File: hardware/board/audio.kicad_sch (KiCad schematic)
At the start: 68 parts, among them J5 LineIn, J6 LineOut, J7 Headphone, U5 TPS7A20xxxDBV, U6 MAX98089ETN_T, Y2 12.288MHz

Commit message: hella footprints and trying out layouts
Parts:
- J5, J6: footprint Connector_Audio:Jack_3.5mm_CUI_SJ-3523-SMT_Horizontal -> Connector_Audio:Jack_3.5mm_CUI_SJ1-3525N_Horizontal
- J7: footprint ledaw:CUI_SJ-43514-SMT-TR -> ledaw:CUI_SJ-43514
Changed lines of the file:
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@@
 			)
 		)
-		(property "Footprint" "Connector_Audio:Jack_3.5mm_CUI_SJ-3523-SMT_Horizontal"
+		(property "Footprint" "Connector_Audio:Jack_3.5mm_CUI_SJ1-3525N_Horizontal"
 			(at 207.01 86.36 0)
 			(hide yes)
@@
 			)
 		)
-		(property "Footprint" "ledaw:CUI_SJ-43514-SMT-TR"
+		(property "Footprint" "ledaw:CUI_SJ-43514"
 			(at 207.01 107.95 0)
 			(hide yes)
@@
 			)
 		)
-		(property "Footprint" "Connector_Audio:Jack_3.5mm_CUI_SJ-3523-SMT_Horizontal"
+		(property "Footprint" "Connector_Audio:Jack_3.5mm_CUI_SJ1-3525N_Horizontal"
 			(at 71.12 107.95 0)
 			(hide yes)

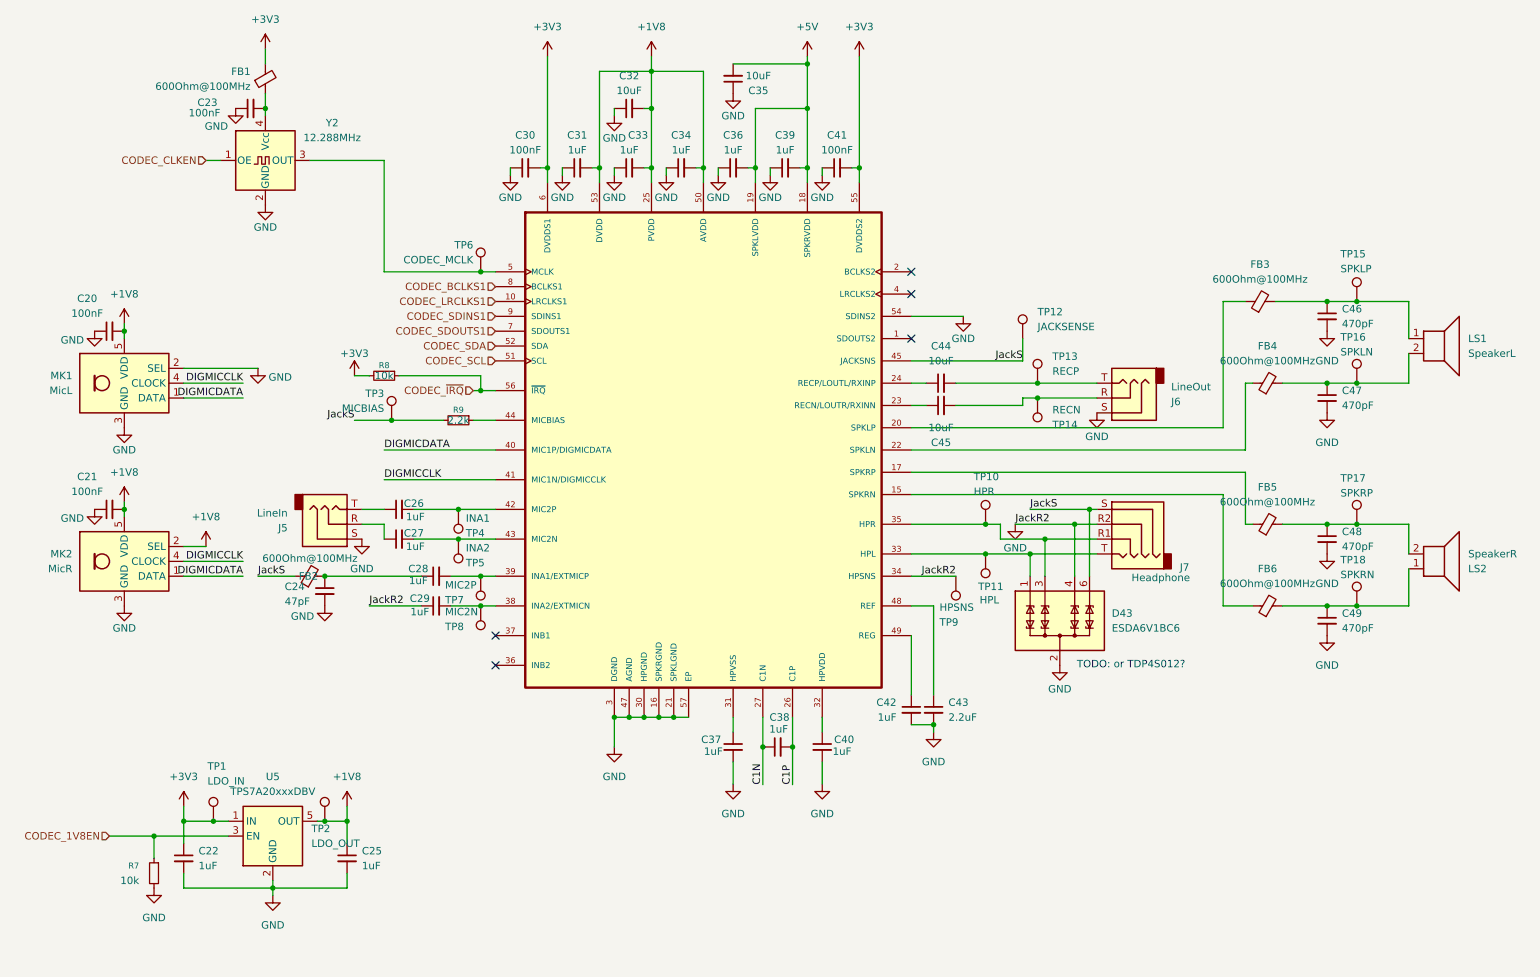
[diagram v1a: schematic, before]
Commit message: fix hpmic / linein mixup
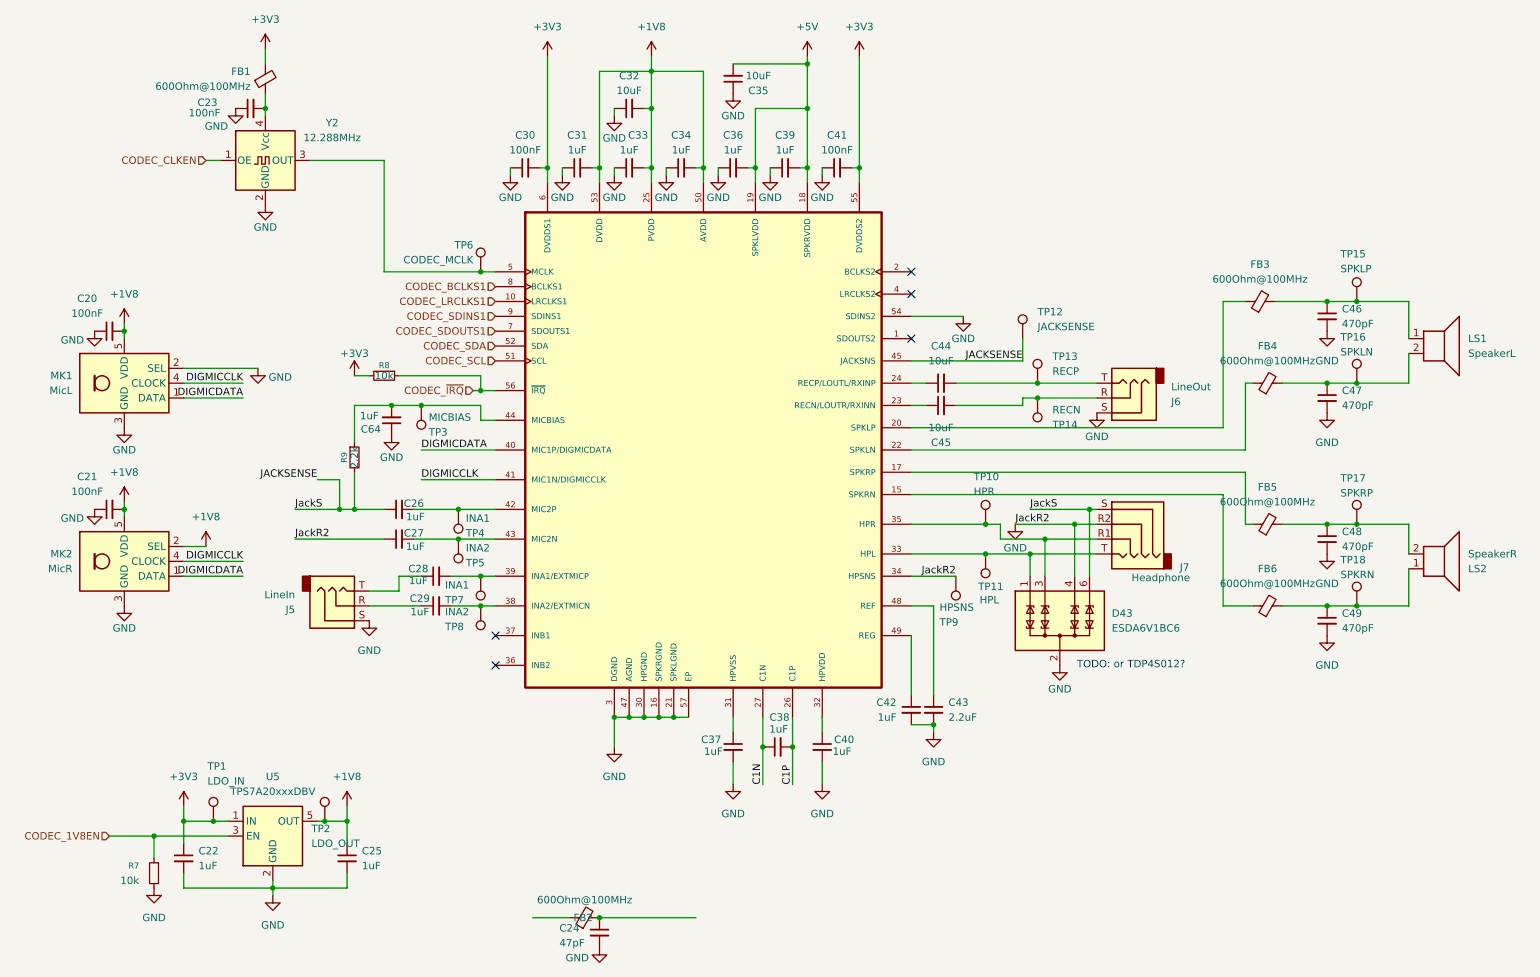
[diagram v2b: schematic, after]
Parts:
- added C64: 1uF, Capacitor_SMD:C_0805_2012Metric, symbol Device:C_Small
- TP7: value MIC2P -> INA1
- TP8: value MIC2N -> INA2
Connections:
- net GND: now also C27.1, C64.1; no longer C29.1
- net at C24.1, FB2.2: no longer C28.1
- net at J5.T: now also C28.1; no longer C26.1
- net at J5.R: now also C29.1; no longer C27.1
- net at R9.1, U6.44 (MICBIAS): now also TP3.1, C64.2
- net JackS renamed JACKSENSE
- net JACKSENSE: now also C26.1; no longer FB2.1, TP3.1

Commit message: reannoation with good linkage?
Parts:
- renumbered C35 to C201, C23 to C202, C32 to C203, C30 to C204, C31 to C205, C33 to C206, C34 to C207, C36 to C208, C39 to C209, C41 to C210, C46 to C211, C20 to C212, C44 to C213, C47 to C214, C45 to C215, C64 to C216, C21 to C217, C26 to C218, C27 to C219, C48 to C220, C28 to C221, C29 to C222, C49 to C223, C42 to C224, C43 to C225, C37 to C226, C38 to C227, C40 to C228, C22 to C229, C25 to C230, C24 to C231, D43 to D201, FB1 to FB201, FB3 to FB202, FB4 to FB203, FB5 to FB204, FB6 to FB205, FB2 to FB206, J6 to J201, J7 to J202, J5 to J203, LS1 to LS201, LS2 to LS202, MK1 to MK201, MK2 to MK202, R8 to R201, R9 to R202, R7 to R203, TP6 to TP201, TP15 to TP202, TP12 to TP203, TP13 to TP204, TP16 to TP205, TP14 to TP206, TP3 to TP207, TP4 to TP208, TP10 to TP209, TP17 to TP210, TP5 to TP211, TP11 to TP212, TP7 to TP213, TP9 to TP214, TP8 to TP215, TP18 to TP216, TP1 to TP217, TP2 to TP218, U6 to U201, U5 to U202, Y2 to Y201

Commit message: wip made a mistake adding micbias cap from hat
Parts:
- renumbered C216 to CX201
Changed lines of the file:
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@@
 		(in_pos_files yes)
 		(dnp no)
-		(property "Reference" "C216"
+		(property "Reference" "CX201"
 			(at 77.724 91.694 0)
 			(show_name no)
@@
 			(project "board"
 				(path "/dd13fd41-39ab-4435-9074-5024f1786746/bead49b4-6be4-481c-a37b-4cba7f02eadb"
-					(reference "C216")
+					(reference "CX201")
 					(unit 1)
 				)

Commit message: i think this is finally right
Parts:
- removed C231: 47pF, Capacitor_SMD:C_0805_2012Metric, symbol Device:C_Small
- removed FB206: 600Ohm@100MHz, Inductor_SMD:L_0805_2012Metric, symbol Device:FerriteBead_Small
- added C230: 47pF, Capacitor_SMD:C_0805_2012Metric, symbol Device:C_Small
- renumbered C217 to C216, C218 to C217, C219 to C218, C220 to C219, C221 to C220, C222 to C221, C223 to C222, C224 to C223, C225 to C224, C226 to C225, C227 to C226, C228 to C227, C229 to C228, C230 to C229

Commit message: speakers?
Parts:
- LS201, LS202: now not fitted
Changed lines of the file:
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@@
 		(on_board yes)
 		(in_pos_files yes)
-		(dnp no)
+		(dnp yes)
 		(property "Reference" "LS202"
 			(at 265.43 115.5701 0)
@@
 		(on_board yes)
 		(in_pos_files yes)
-		(dnp no)
+		(dnp yes)
 		(property "Reference" "LS201"
 			(at 265.43 76.1999 0)

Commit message: some big tim routing
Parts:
- renumbered C230 to C221, C221 to C222, C222 to C223, C223 to C224, C224 to C225, C225 to C226, C226 to C227, C227 to C228, C228 to C229, C229 to C230
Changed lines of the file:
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@@
 		(in_pos_files yes)
 		(dnp no)
-		(property "Reference" "C223"
+		(property "Reference" "C224"
 			(at 167.64 138.4362 0)
 			(show_name no)
@@
 			(project "board"
 				(path "/dd13fd41-39ab-4435-9074-5024f1786746/bead49b4-6be4-481c-a37b-4cba7f02eadb"
-					(reference "C223")
+					(reference "C224")
 					(unit 1)
 				)
@@
 		(in_pos_files yes)
 		(dnp no)
-		(property "Reference" "C225"
+		(property "Reference" "C226"
 			(at 137.668 144.78 0)
 			(show_name no)
@@
 			(project "board"
 				(path "/dd13fd41-39ab-4435-9074-5024f1786746/bead49b4-6be4-481c-a37b-4cba7f02eadb"
-					(reference "C225")
+					(reference "C226")
 					(unit 1)
 				)
@@
 		(in_pos_files yes)
 		(dnp no)
-		(property "Reference" "C227"
+		(property "Reference" "C228"
 			(at 156.972 144.78 0)
 			(show_name no)
@@
 			(project "board"
 				(path "/dd13fd41-39ab-4435-9074-5024f1786746/bead49b4-6be4-481c-a37b-4cba7f02eadb"
-					(reference "C227")
+					(reference "C228")
 					(unit 1)
 				)
@@
 		(dnp no)
 		(fields_autoplaced yes)
-		(property "Reference" "C222"
+		(property "Reference" "C223"
 			(at 243.84 123.1962 0)
 			(show_name no)
@@
 			(project "board"
 				(path "/dd13fd41-39ab-4435-9074-5024f1786746/bead49b4-6be4-481c-a37b-4cba7f02eadb"
-					(reference "C222")
+					(reference "C223")
 					(unit 1)
 				)
@@
 		(in_pos_files yes)
 		(dnp no)
-		(property "Reference" "C230"
+		(property "Reference" "C221"
 			(at 49.022 119.888 0)
 			(show_name no)
@@
 			(project "board"
 				(path "/dd13fd41-39ab-4435-9074-5024f1786746/bead49b4-6be4-481c-a37b-4cba7f02eadb"
-					(reference "C230")
+					(reference "C221")
 					(unit 1)
 				)
@@
 		(dnp no)
 		(fields_autoplaced yes)
-		(property "Reference" "C229"
+		(property "Reference" "C230"
 			(at 76.2 163.8362 0)
 			(show_name no)
@@
 			(project "board"
 				(path "/dd13fd41-39ab-4435-9074-5024f1786746/bead49b4-6be4-481c-a37b-4cba7f02eadb"
-					(reference "C229")
+					(reference "C230")
 					(unit 1)
 				)
@@
 		(dnp no)
 		(fields_autoplaced yes)
-		(property "Reference" "C224"
+		(property "Reference" "C225"
 			(at 176.53 138.4362 0)
 			(show_name no)
@@
 			(project "board"
 				(path "/dd13fd41-39ab-4435-9074-5024f1786746/bead49b4-6be4-481c-a37b-4cba7f02eadb"
-					(reference "C224")
+					(reference "C225")
 					(unit 1)
 				)
@@
 		(in_pos_files yes)
 		(dnp no)
-		(property "Reference" "C226"
+		(property "Reference" "C227"
 			(at 149.352 140.97 90)
 			(show_name no)
@@
 			(project "board"
 				(path "/dd13fd41-39ab-4435-9074-5024f1786746/bead49b4-6be4-481c-a37b-4cba7f02eadb"
-					(reference "C226")
+					(reference "C227")
 					(unit 1)
 				)
@@
 		(dnp no)
 		(fields_autoplaced yes)
-		(property "Reference" "C228"
+		(property "Reference" "C229"
 			(at 48.26 163.8362 0)
 			(show_name no)
@@
 			(project "board"
 				(path "/dd13fd41-39ab-4435-9074-5024f1786746/bead49b4-6be4-481c-a37b-4cba7f02eadb"
-					(reference "C228")
+					(reference "C229")
 					(unit 1)
 				)
@@
 		(in_pos_files yes)
 		(dnp no)
-		(property "Reference" "C221"
+		(property "Reference" "C222"
 			(at 86.106 120.65 90)
 			(show_name no)
@@
 			(project "board"
 				(path "/dd13fd41-39ab-4435-9074-5024f1786746/bead49b4-6be4-481c-a37b-4cba7f02eadb"
-					(reference "C221")
+					(reference "C222")
 					(unit 1)
 				)

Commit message: pre accidentally messed up the references
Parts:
- removed C221: 47pF, Capacitor_SMD:C_0805_2012Metric, symbol Device:C_Small
- renumbered C222 to C221, C223 to C222, C224 to C223, C225 to C224, C226 to C225, C227 to C226, C228 to C227, C229 to C228, C230 to C229
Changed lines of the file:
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@@
 		(in_pos_files yes)
 		(dnp no)
-		(property "Reference" "C224"
+		(property "Reference" "C223"
 			(at 167.64 138.4362 0)
 			(show_name no)
@@
 			(project "board"
 				(path "/dd13fd41-39ab-4435-9074-5024f1786746/bead49b4-6be4-481c-a37b-4cba7f02eadb"
-					(reference "C224")
+					(reference "C223")
 					(unit 1)
 				)
@@
 		(in_pos_files yes)
 		(dnp no)
-		(property "Reference" "C226"
+		(property "Reference" "C225"
 			(at 137.668 144.78 0)
 			(show_name no)
@@
 			(project "board"
 				(path "/dd13fd41-39ab-4435-9074-5024f1786746/bead49b4-6be4-481c-a37b-4cba7f02eadb"
-					(reference "C226")
+					(reference "C225")
 					(unit 1)
 				)
@@
 		(in_pos_files yes)
 		(dnp no)
-		(property "Reference" "C228"
+		(property "Reference" "C227"
 			(at 156.972 144.78 0)
 			(show_name no)
@@
 			(project "board"
 				(path "/dd13fd41-39ab-4435-9074-5024f1786746/bead49b4-6be4-481c-a37b-4cba7f02eadb"
-					(reference "C228")
+					(reference "C227")
 					(unit 1)
 				)
@@
 		(dnp no)
 		(fields_autoplaced yes)
-		(property "Reference" "C223"
+		(property "Reference" "C222"
 			(at 243.84 123.1962 0)
 			(show_name no)
@@
 			(project "board"
 				(path "/dd13fd41-39ab-4435-9074-5024f1786746/bead49b4-6be4-481c-a37b-4cba7f02eadb"
-					(reference "C223")
+					(reference "C222")
 					(unit 1)
 				)
@@
 	)
 	(symbol
-		(lib_id "Device:C_Small")
-		(at 55.88 120.65 0)
-		(unit 1)
-		(body_style 1)
-		(exclude_from_sim no)
-		(in_bom yes)
-		(on_board yes)
-		(in_pos_files yes)
-		(dnp no)
-		(property "Reference" "C221"
-			(at 49.022 119.888 0)
-			(show_name no)
-			(do_not_autoplace no)
-			(effects
-				(font
-					(size 1.27 1.27)
-				)
-				(justify left)
-			)
-		)
-		(property "Value" "47pF"
-			(at 49.022 122.428 0)
-			(show_name no)
-			(do_not_autoplace no)
-			(effects
-				(font
-					(size 1.27 1.27)
-				)
-				(justify left)
-			)
-		)
-		(property "Footprint" "Capacitor_SMD:C_0805_2012Metric"
-			(at 55.88 120.65 0)
-			(hide yes)
-			(show_name no)
-			(do_not_autoplace no)
-			(effects
-				(font
-					(size 1.27 1.27)
-				)
-			)
-		)
-		(property "Datasheet" ""
-			(at 55.88 120.65 0)
-			(hide yes)
-			(show_name no)
-			(do_not_autoplace no)
-			(effects
-				(font
-					(size 1.27 1.27)
-				)
-			)
-		)
-		(property "Description" "Unpolarized capacitor, small symbol"
-			(at 55.88 120.65 0)
-			(hide yes)
-			(show_name no)
-			(do_not_autoplace no)
-			(effects
-				(font
-					(size 1.27 1.27)
-				)
-			)
-		)
-		(property "LCSC" "C14857"
-			(at 55.88 120.65 0)
-			(hide yes)
-			(show_name no)
-			(do_not_autoplace no)
-			(effects
-				(font
-					(size 1.27 1.27)
-				)
-			)
-		)
-		(pin "1"
-		)
-		(pin "2"
-		)
-		(instances
-			(project "board"
-				(path "/dd13fd41-39ab-4435-9074-5024f1786746/bead49b4-6be4-481c-a37b-4cba7f02eadb"
-					(reference "C221")
-					(unit 1)
-				)
-			)
-		)
-	)
-	(symbol
 		(lib_id "Connector:TestPoint")
 		(at 96.52 116.84 180)
@@
 		(dnp no)
 		(fields_autoplaced yes)
-		(property "Reference" "C230"
+		(property "Reference" "C229"
 			(at 76.2 163.8362 0)
 			(show_name no)
@@
 			(project "board"
 				(path "/dd13fd41-39ab-4435-9074-5024f1786746/bead49b4-6be4-481c-a37b-4cba7f02eadb"
-					(reference "C230")
+					(reference "C229")
 					(unit 1)
 				)
@@
 		(dnp no)
 		(fields_autoplaced yes)
-		(property "Reference" "C225"
+		(property "Reference" "C224"
 			(at 176.53 138.4362 0)
 			(show_name no)
@@
 			(project "board"
 				(path "/dd13fd41-39ab-4435-9074-5024f1786746/bead49b4-6be4-481c-a37b-4cba7f02eadb"
-					(reference "C225")
+					(reference "C224")
 					(unit 1)
 				)
@@
 		(in_pos_files yes)
 		(dnp no)
-		(property "Reference" "C227"
+		(property "Reference" "C226"
 			(at 149.352 140.97 90)
 			(show_name no)
@@
 			(project "board"
 				(path "/dd13fd41-39ab-4435-9074-5024f1786746/bead49b4-6be4-481c-a37b-4cba7f02eadb"
-					(reference "C227")
+					(reference "C226")
 					(unit 1)
 				)
@@
 		(dnp no)
 		(fields_autoplaced yes)
-		(property "Reference" "C229"
+		(property "Reference" "C228"
 			(at 48.26 163.8362 0)
 			(show_name no)
@@
 			(project "board"
 				(path "/dd13fd41-39ab-4435-9074-5024f1786746/bead49b4-6be4-481c-a37b-4cba7f02eadb"
-					(reference "C229")
+					(reference "C228")
 					(unit 1)
 				)
@@
 		(in_pos_files yes)
 		(dnp no)
-		(property "Reference" "C222"
+		(property "Reference" "C221"
 			(at 86.106 120.65 90)
 			(show_name no)
@@
 			(project "board"
 				(path "/dd13fd41-39ab-4435-9074-5024f1786746/bead49b4-6be4-481c-a37b-4cba7f02eadb"
-					(reference "C222")
+					(reference "C221")
 					(unit 1)
 				)
